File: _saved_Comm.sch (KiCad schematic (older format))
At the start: 16 parts, among them P201 CONN_01X06, P202 CONN_01X04, P203 CONN_01X04, P204 CONN_01X03, P205 CONN_01X02, SW201 SW_PUSH

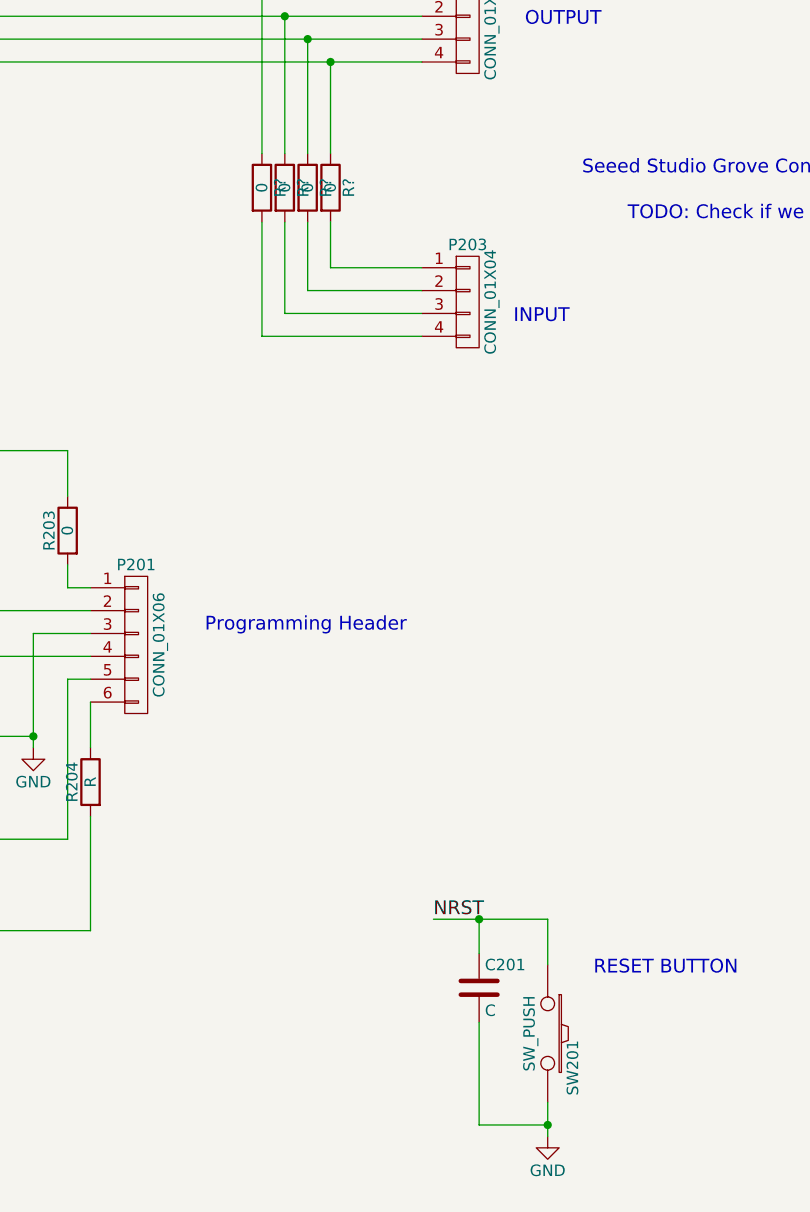
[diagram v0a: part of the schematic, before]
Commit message: Added ground and power layers.
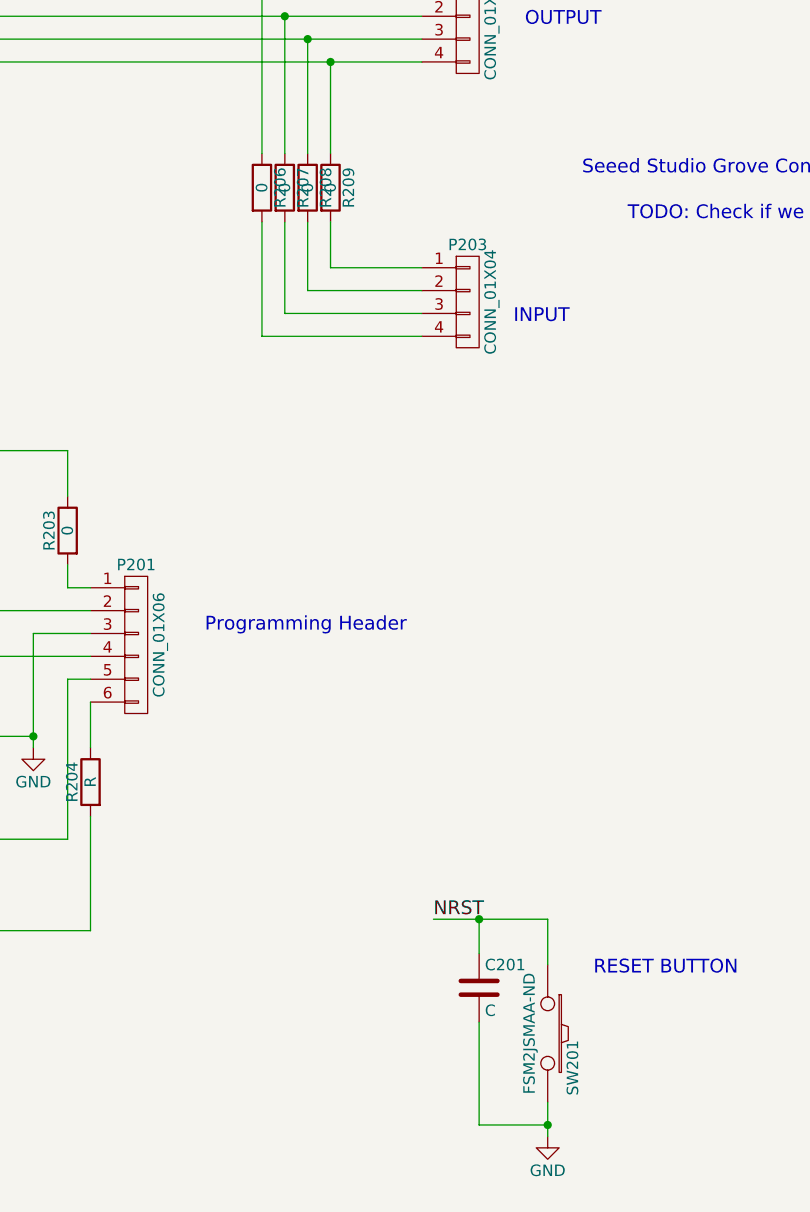
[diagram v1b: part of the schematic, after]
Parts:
- R206, R207, R208, R209: renamed from R?; footprint (none) -> Resistors_SMD:R_0805
- SW201: value SW_PUSH -> FSM2JSMAA-ND; footprint Buttons_Switches_ThroughHole:SW_PUSH_SMALL -> CentralCommand:FSM2JSMAA-ND
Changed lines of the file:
@@
 $EndComp
 $Comp
-L GND #PWR04
+L GND #PWR05
 U 1 1 565FC7CA
 P 3500 4500
-F 0 "#PWR04" H 3500 4250 50  0001 C CNN
+F 0 "#PWR05" H 3500 4250 50  0001 C CNN
 F 1 "GND" H 3500 4350 50  0000 C CNN
 F 2 "" H 3500 4500 60  0000 C CNN
@@
 P 5750 5750
 F 0 "SW201" H 5900 5860 50  0000 C CNN
-F 1 "SW_PUSH" H 5750 5670 50  0000 C CNN
-F 2 "Buttons_Switches_ThroughHole:SW_PUSH_SMALL" H 5750 5750 60  0001 C CNN
-F 3 "" H 5750 5750 60  0000 C CNN
+F 1 "FSM2JSMAA-ND" H 5750 5670 50  0000 C CNN
+F 2 "CentralCommand:FSM2JSMAA-ND" H 5750 5750 60  0001 C CNN
+F 3 "http://www.digikey.com/product-detail/en/FSM2JSMAA/FSM2JSMAA-ND/2400228" H 5750 5750 60  0001 C CNN
 	1    5750 5750
 	0    1    1    0
 $EndComp
 $Comp
-L GND #PWR05
+L GND #PWR06
 U 1 1 565FED52
 P 5750 6200
-F 0 "#PWR05" H 5750 5950 50  0001 C CNN
+F 0 "#PWR06" H 5750 5950 50  0001 C CNN
 F 1 "GND" H 5750 6050 50  0000 C CNN
 F 2 "" H 5750 6200 60  0000 C CNN
@@
 $EndComp
 $Comp
-L GND #PWR06
+L GND #PWR07
 U 1 1 5660DBDE
 P 9550 5400
-F 0 "#PWR06" H 9550 5150 50  0001 C CNN
+F 0 "#PWR07" H 9550 5150 50  0001 C CNN
 F 1 "GND" H 9550 5250 50  0000 C CNN
 F 2 "" H 9550 5400 60  0000 C CNN
@@
 	7450 5950 7450 6250
 $Comp
-L GND #PWR07
+L GND #PWR08
 U 1 1 5661772D
 P 7450 6250
-F 0 "#PWR07" H 7450 6000 50  0001 C CNN
+F 0 "#PWR08" H 7450 6000 50  0001 C CNN
 F 1 "GND" H 7450 6100 50  0000 C CNN
 F 2 "" H 7450 6250 60  0000 C CNN
@@
 	2250 1500 5200 1500
 $Comp
-L R R?
+L R R209
 U 1 1 56691488
 P 4800 2050
-F 0 "R?" V 4880 2050 50  0000 C CNN
+F 0 "R209" V 4880 2050 50  0000 C CNN
 F 1 "0" V 4800 2050 50  0000 C CNN
-F 2 "" V 4730 2050 30  0000 C CNN
+F 2 "Resistors_SMD:R_0805" V 4730 2050 30  0001 C CNN
 F 3 "" H 4800 2050 30  0000 C CNN
 	1    4800 2050
@@
 Connection ~ 4800 1500
 $Comp
-L R R?
+L R R208
 U 1 1 566915C1
 P 4700 2050
-F 0 "R?" V 4780 2050 50  0000 C CNN
+F 0 "R208" V 4780 2050 50  0000 C CNN
 F 1 "0" V 4700 2050 50  0000 C CNN
-F 2 "" V 4630 2050 30  0000 C CNN
+F 2 "Resistors_SMD:R_0805" V 4630 2050 30  0001 C CNN
 F 3 "" H 4700 2050 30  0000 C CNN
 	1    4700 2050
@@
 	4700 2500 4700 2200
 $Comp
-L R R?
+L R R207
 U 1 1 56691697
 P 4600 2050
-F 0 "R?" V 4680 2050 50  0000 C CNN
+F 0 "R207" V 4680 2050 50  0000 C CNN
 F 1 "0" V 4600 2050 50  0000 C CNN
-F 2 "" V 4530 2050 30  0000 C CNN
+F 2 "Resistors_SMD:R_0805" V 4530 2050 30  0001 C CNN
 F 3 "" H 4600 2050 30  0000 C CNN
 	1    4600 2050
@@
 Connection ~ 4700 1400
 $Comp
-L R R?
+L R R206
 U 1 1 56691864
 P 4500 2050
-F 0 "R?" V 4580 2050 50  0000 C CNN
+F 0 "R206" V 4580 2050 50  0000 C CNN
 F 1 "0" V 4500 2050 50  0000 C CNN
-F 2 "" V 4430 2050 30  0000 C CNN
+F 2 "Resistors_SMD:R_0805" V 4430 2050 30  0001 C CNN
 F 3 "" H 4500 2050 30  0000 C CNN
 	1    4500 2050
